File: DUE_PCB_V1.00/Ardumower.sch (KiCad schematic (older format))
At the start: 50 parts, among them J1 9V IN, J10 Sonar_R, J11 Sonar_C, J12 Sonar_L, J13 P_Right, J14 DS3231 RTC, J15 Button, J16 Button, J17 Button, J18 Button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

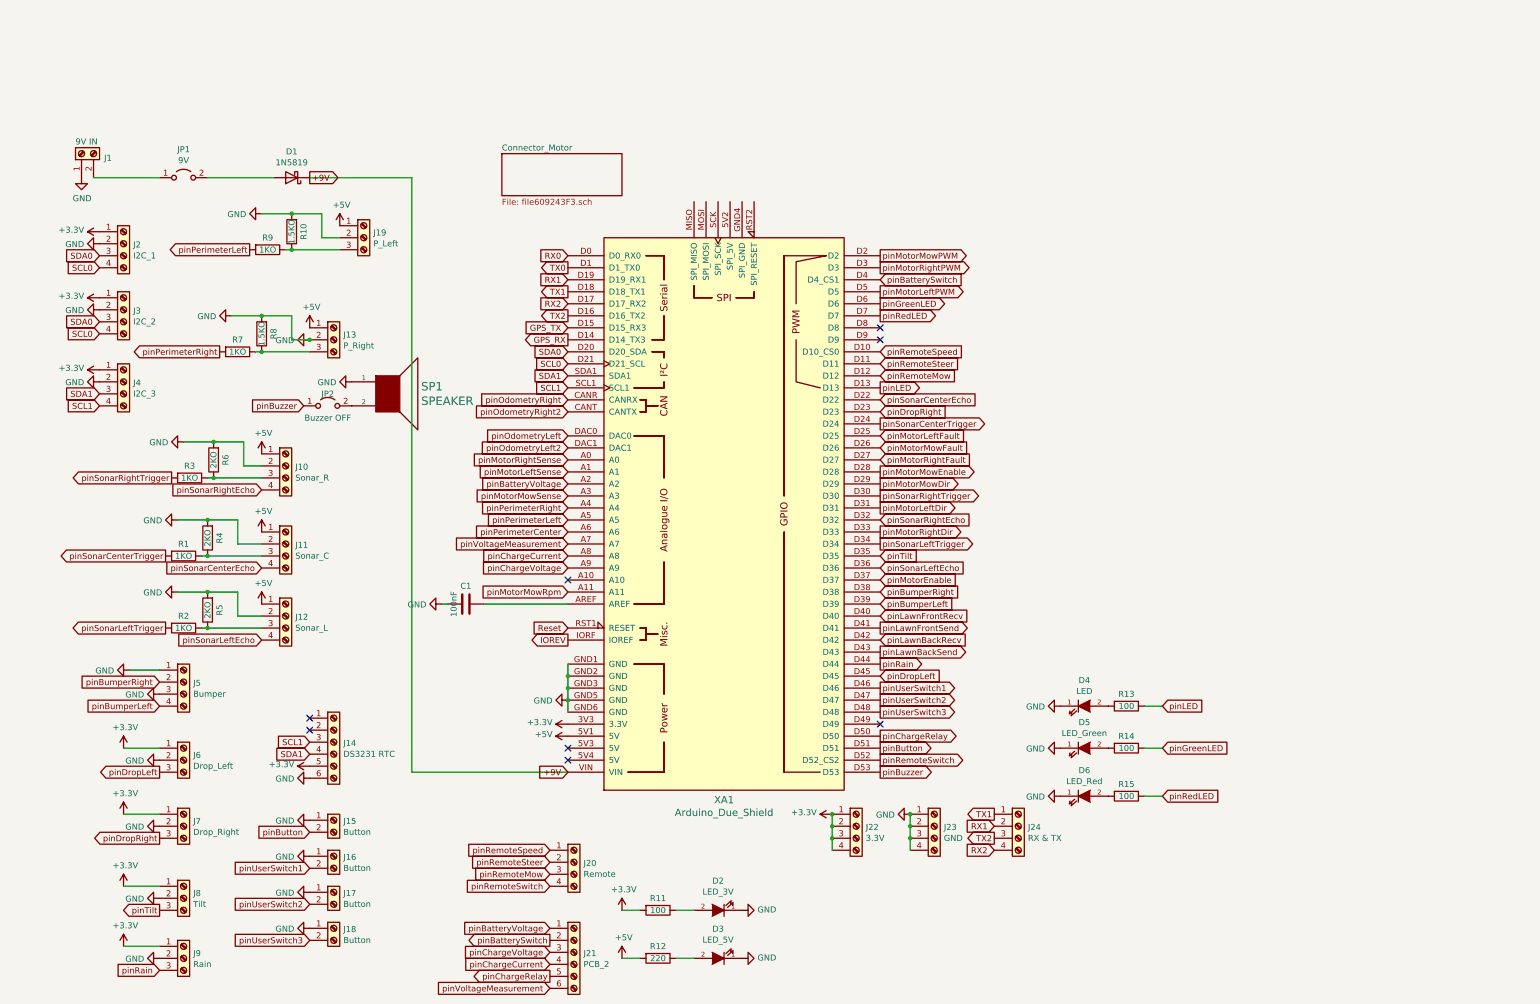
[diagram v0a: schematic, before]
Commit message: Add Power Source
Add Power Source for 5V & 3.3V
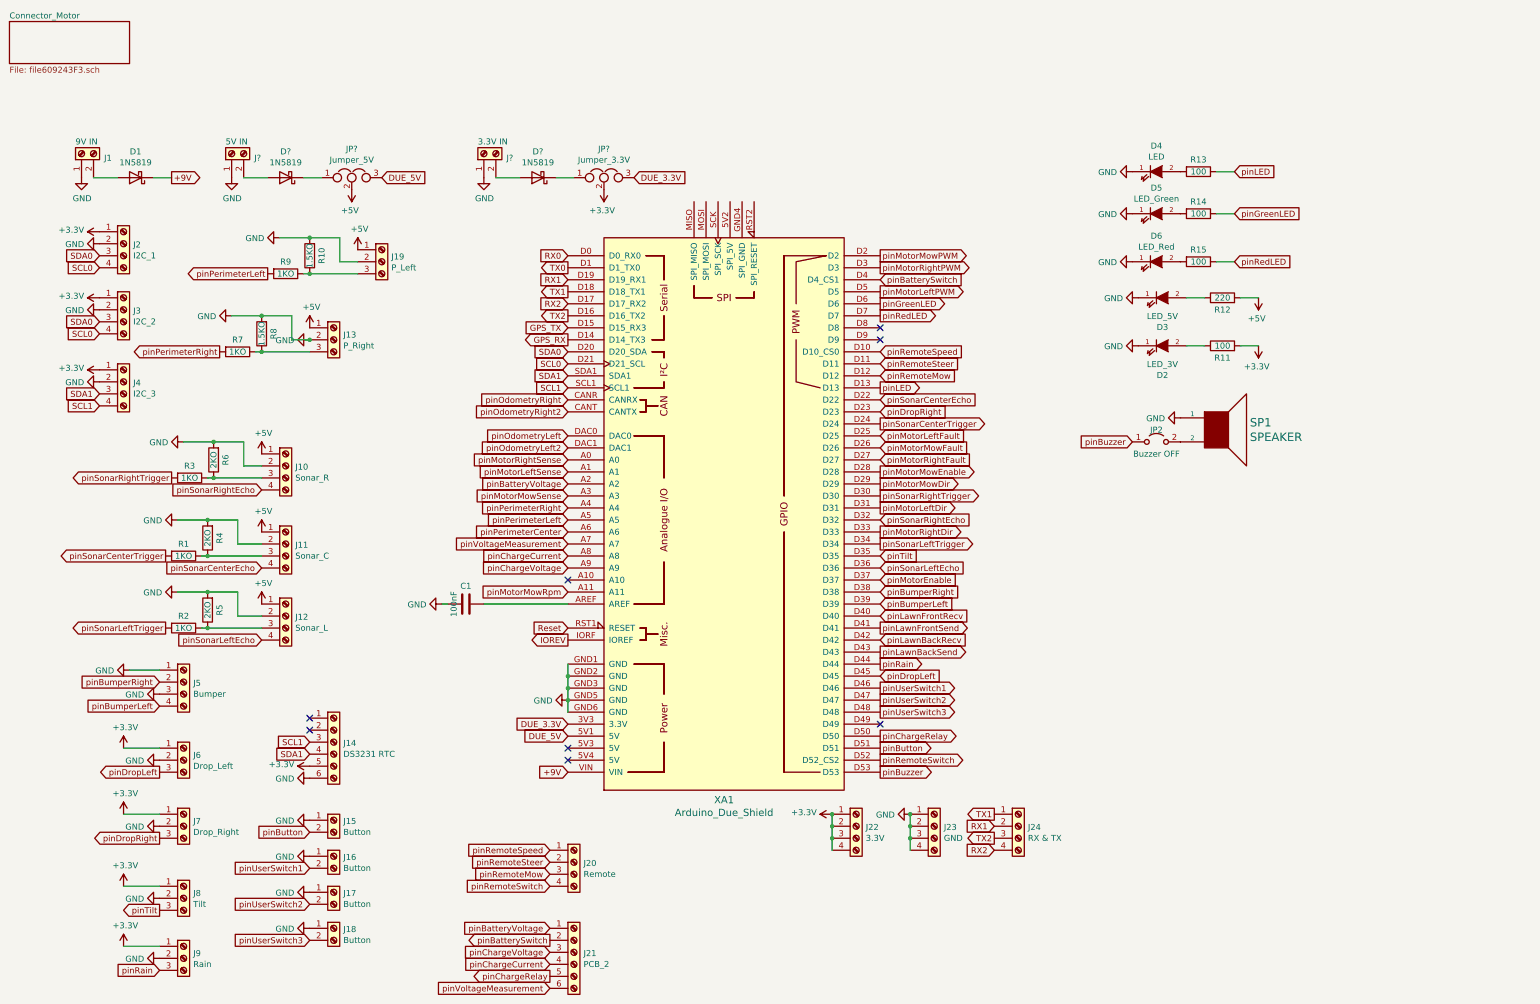
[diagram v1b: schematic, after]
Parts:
- removed JP1: 9V, Connector_PinHeader_2.54mm:PinHeader_1x02_P2.54mm_Vertical, symbol Jumper:Jumper_2_Open
- added D? (x2): 1N5819, Diode_THT:D_DO-41_SOD81_P10.16mm_Horizontal, symbol Diode:1N5819
- added J?: 5V IN, TerminalBlock:TerminalBlock_bornier-2_P5.08mm, symbol Connector:Screw_Terminal_01x02
- added J?: 3.3V IN, TerminalBlock:TerminalBlock_bornier-2_P5.08mm, symbol Connector:Screw_Terminal_01x02
- added JP?: Jumper_5V, symbol Device:Jumper_NC_Dual
- added JP?: Jumper_3.3V, symbol Device:Jumper_NC_Dual
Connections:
- net +3V3: now also JP?.2; no longer XA1.3V3 (3.3V)
- net +5V: now also JP?.2; no longer XA1.5V1 (5V)
- net GND: now also J?.1 (Pin_1), J?.1 (Pin_1)
- net at J1.2 (Pin_2): now also D1.2 (A)
- new net: D?.2 (A), J?.2 (Pin_2) (x2)
- new net: D?.1 (K), JP?.1 (x2)
- new net DUE_3.3V: JP?.3, XA1.3V3 (3.3V)
- new net DUE_5V: JP?.3, XA1.5V1 (5V)
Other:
- moved on the sheet: D1, D2, D3, D4, D5, D6, J19, JP2, R10, R11, R12, R13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

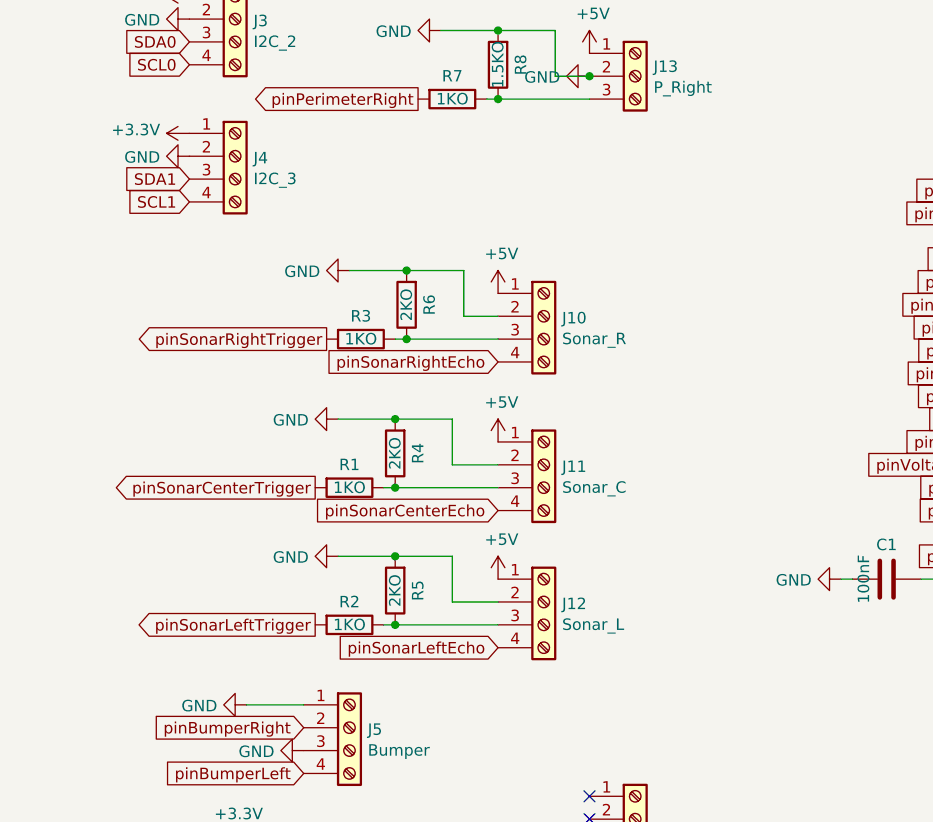
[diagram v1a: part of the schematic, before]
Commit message: Remove Sonar Resistors
Remove Sonar Resistors and change Power Source to 3.3V
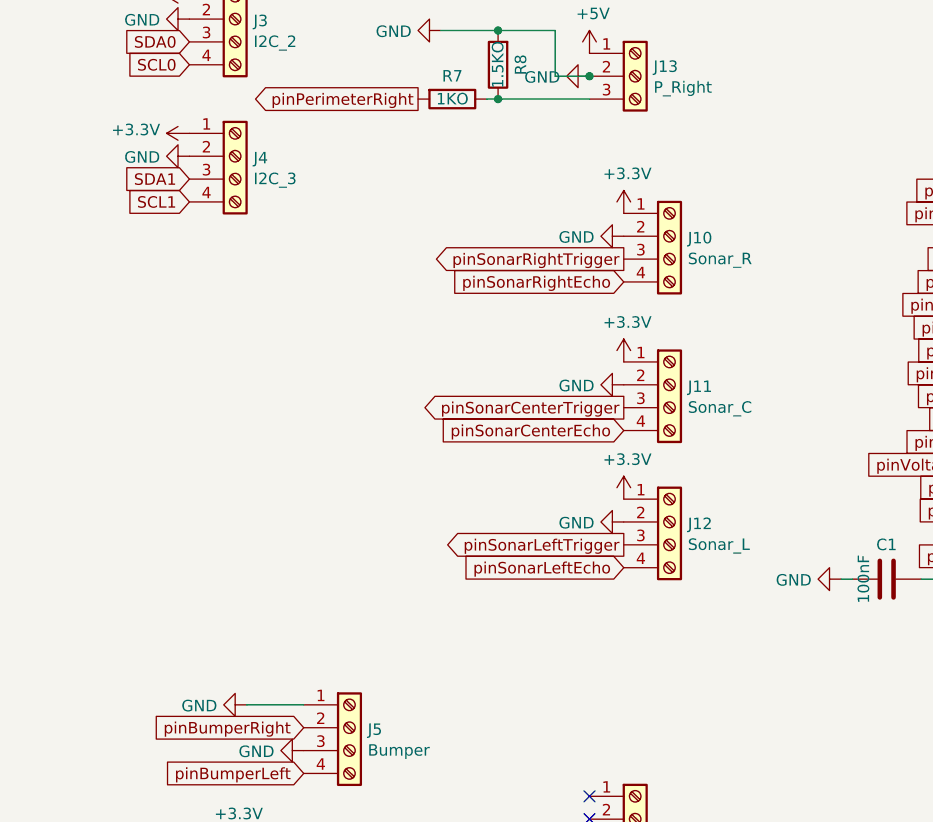
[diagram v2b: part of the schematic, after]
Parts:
- removed R1, R2, R3: 1KO, Resistor_THT:R_Axial_DIN0207_L6.3mm_D2.5mm_P2.54mm_Vertical, symbol Device:R
- removed R4, R5, R6: 2KO, Resistor_THT:R_Axial_DIN0207_L6.3mm_D2.5mm_P2.54mm_Vertical, symbol Device:R
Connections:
- net +3V3: now also J10.1 (Pin_1), J11.1 (Pin_1), J12.1 (Pin_1)
- net +5V: no longer J10.1 (Pin_1), J11.1 (Pin_1), J12.1 (Pin_1)
- net pinSonarCenterTrigger: now also J11.3 (Pin_3)
- net pinSonarLeftTrigger: now also J12.3 (Pin_3)
- net pinSonarRightTrigger: now also J10.3 (Pin_3)
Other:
- moved on the sheet: J10, J11, J12
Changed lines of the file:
@@
 L Connector:Screw_Terminal_01x04 J10
 U 1 1 60757000
-P 2500 3250
-F 0 "J10" H 2580 3242 50  0000 L CNN
-F 1 "Sonar_R" H 2580 3151 50  0000 L CNN
-F 2 "Connector_PinHeader_2.54mm:PinHeader_1x04_P2.54mm_Vertical" H 2500 3250 50  0001 C CNN
-F 3 "~" H 2500 3250 50  0001 C CNN
-	1    2500 3250
+P 3050 2900
+F 0 "J10" H 3130 2892 50  0000 L CNN
+F 1 "Sonar_R" H 3130 2801 50  0000 L CNN
+F 2 "Connector_PinHeader_2.54mm:PinHeader_1x04_P2.54mm_Vertical" H 3050 2900 50  0001 C CNN
+F 3 "~" H 3050 2900 50  0001 C CNN
+	1    3050 2900
 	1    0    0    -1
 $EndComp
@@
 L Connector:Screw_Terminal_01x04 J11
 U 1 1 607583E5
-P 2500 3900
-F 0 "J11" H 2580 3892 50  0000 L CNN
-F 1 "Sonar_C" H 2580 3801 50  0000 L CNN
-F 2 "Connector_PinHeader_2.54mm:PinHeader_1x04_P2.54mm_Vertical" H 2500 3900 50  0001 C CNN
-F 3 "~" H 2500 3900 50  0001 C CNN
-	1    2500 3900
+P 3050 3550
+F 0 "J11" H 3130 3542 50  0000 L CNN
+F 1 "Sonar_C" H 3130 3451 50  0000 L CNN
+F 2 "Connector_PinHeader_2.54mm:PinHeader_1x04_P2.54mm_Vertical" H 3050 3550 50  0001 C CNN
+F 3 "~" H 3050 3550 50  0001 C CNN
+	1    3050 3550
 	1    0    0    -1
 $EndComp
@@
 L Connector:Screw_Terminal_01x04 J12
 U 1 1 60758E5B
-P 2500 4500
-F 0 "J12" H 2580 4492 50  0000 L CNN
-F 1 "Sonar_L" H 2580 4401 50  0000 L CNN
-F 2 "Connector_PinHeader_2.54mm:PinHeader_1x04_P2.54mm_Vertical" H 2500 4500 50  0001 C CNN
-F 3 "~" H 2500 4500 50  0001 C CNN
-	1    2500 4500
-	1    0    0    -1
-$EndComp
-$Comp
-L power:+5V #PWR024
-U 1 1 6075A993
-P 2300 3800
-F 0 "#PWR024" H 2300 3650 50  0001 C CNN
-F 1 "+5V" H 2315 3973 50  0000 C CNN
-F 2 "" H 2300 3800 50  0001 C CNN
-F 3 "" H 2300 3800 50  0001 C CNN
-	1    2300 3800
-	1    0    0    -1
-$EndComp
-$Comp
-L power:+5V #PWR025
-U 1 1 6075B07F
-P 2300 4400
-F 0 "#PWR025" H 2300 4250 50  0001 C CNN
-F 1 "+5V" H 2315 4573 50  0000 C CNN
-F 2 "" H 2300 4400 50  0001 C CNN
-F 3 "" H 2300 4400 50  0001 C CNN
-	1    2300 4400
-	1    0    0    -1
-$EndComp
-Text GLabel 2300 4100 0    50   Input ~ 0
+P 3050 4150
+F 0 "J12" H 3130 4142 50  0000 L CNN
+F 1 "Sonar_L" H 3130 4051 50  0000 L CNN
+F 2 "Connector_PinHeader_2.54mm:PinHeader_1x04_P2.54mm_Vertical" H 3050 4150 50  0001 C CNN
+F 3 "~" H 3050 4150 50  0001 C CNN
+	1    3050 4150
+	1    0    0    -1
+$EndComp
+Text GLabel 2850 3750 0    50   Input ~ 0
 pinSonarCenterEcho
-Text GLabel 2300 3450 0    50   Input ~ 0
+Text GLabel 2850 3100 0    50   Input ~ 0
 pinSonarRightEcho
-Text GLabel 2300 4700 0    50   Input ~ 0
+Text GLabel 2850 4350 0    50   Input ~ 0
 pinSonarLeftEcho
 $Comp
@@
 L power:GND #PWR018
 U 1 1 6097F3DC
-P 1600 3700
-F 0 "#PWR018" H 1600 3450 50  0001 C CNN
-F 1 "GND" V 1605 3572 50  0000 R CNN
-F 2 "" H 1600 3700 50  0001 C CNN
-F 3 "" H 1600 3700 50  0001 C CNN
-	1    1600 3700
+P 2850 3550
+F 0 "#PWR018" H 2850 3300 50  0001 C CNN
+F 1 "GND" V 2855 3422 50  0000 R CNN
+F 2 "" H 2850 3550 50  0001 C CNN
+F 3 "" H 2850 3550 50  0001 C CNN
+	1    2850 3550
 	0    1    1    0
 $EndComp
@@
 NoConn ~ 7450 5400
 NoConn ~ 7450 2200
-Wire Wire Line
-	2100 3700 2100 3900
-Wire Wire Line
-	2100 3900 2300 3900
 $Comp
 L power:GND #PWR019
 U 1 1 60A92EB8
-P 1600 4300
-F 0 "#PWR019" H 1600 4050 50  0001 C CNN
-F 1 "GND" V 1605 4172 50  0000 R CNN
-F 2 "" H 1600 4300 50  0001 C CNN
-F 3 "" H 1600 4300 50  0001 C CNN
-	1    1600 4300
-	0    1    1    0
-$EndComp
-Wire Wire Line
-	2100 4300 2100 4500
-Wire Wire Line
-	2100 4500 2300 4500
+P 2850 4150
+F 0 "#PWR019" H 2850 3900 50  0001 C CNN
+F 1 "GND" V 2855 4022 50  0000 R CNN
+F 2 "" H 2850 4150 50  0001 C CNN
+F 3 "" H 2850 4150 50  0001 C CNN
+	1    2850 4150
+	0    1    1    0
+$EndComp
 $Comp
 L power:GND #PWR020
 U 1 1 60A9B8D5
-P 1650 3050
-F 0 "#PWR020" H 1650 2800 50  0001 C CNN
-F 1 "GND" V 1655 2922 50  0000 R CNN
-F 2 "" H 1650 3050 50  0001 C CNN
-F 3 "" H 1650 3050 50  0001 C CNN
-	1    1650 3050
-	0    1    1    0
-$EndComp
-Wire Wire Line
-	2150 3050 2150 3250
-Wire Wire Line
-	2150 3250 2300 3250
-$Comp
-L power:+5V #PWR023
-U 1 1 60AAE1DB
-P 2300 3150
-F 0 "#PWR023" H 2300 3000 50  0001 C CNN
-F 1 "+5V" H 2315 3323 50  0000 C CNN
-F 2 "" H 2300 3150 50  0001 C CNN
-F 3 "" H 2300 3150 50  0001 C CNN
-	1    2300 3150
-	1    0    0    -1
+P 2850 2900
+F 0 "#PWR020" H 2850 2650 50  0001 C CNN
+F 1 "GND" V 2855 2772 50  0000 R CNN
+F 2 "" H 2850 2900 50  0001 C CNN
+F 3 "" H 2850 2900 50  0001 C CNN
+	1    2850 2900
+	0    1    1    0
 $EndComp
 Text GLabel 7450 1500 2    50   Output ~ 0
@@
 Text GLabel 4850 4300 0    50   Input ~ 0
 pinMotorMowRpm
-Wire Wire Line
-	2150 3050 1900 3050
-Wire Wire Line
-	1650 3050 1900 3050
-Connection ~ 1900 3050
-Wire Wire Line
-	2300 3350 1900 3350
-Connection ~ 1900 3350
-$Comp
-L Device:R R6
-U 1 1 60A9C277
-P 1900 3200
-F 0 "R6" V 1800 3200 50  0000 C CNN
-F 1 "2KO" V 1900 3200 50  0000 C CNN
-F 2 "Resistor_THT:R_Axial_DIN0207_L6.3mm_D2.5mm_P2.54mm_Vertical" V 1830 3200 50  0001 C CNN
-F 3 "~" H 1900 3200 50  0001 C CNN
-	1    1900 3200
-	-1   0    0    1
-$EndComp
-Wire Wire Line
-	1850 3350 1900 3350
-$Comp
-L Device:R R3
-U 1 1 60A9C26D
-P 1700 3350
-F 0 "R3" V 1600 3350 50  0000 C CNN
-F 1 "1KO" V 1700 3350 50  0000 C CNN
-F 2 "Resistor_THT:R_Axial_DIN0207_L6.3mm_D2.5mm_P2.54mm_Vertical" V 1630 3350 50  0001 C CNN
-F 3 "~" H 1700 3350 50  0001 C CNN
-	1    1700 3350
-	0    1    1    0
-$EndComp
-Text GLabel 1550 3350 0    50   Output ~ 0
+Text GLabel 2850 3000 0    50   Output ~ 0
 pinSonarRightTrigger
-Wire Wire Line
-	1600 3700 1850 3700
-Wire Wire Line
-	2100 3700 1850 3700
-Connection ~ 1850 3700
-Wire Wire Line
-	2300 4000 1850 4000
-$Comp
-L Device:R R4
-U 1 1 60A59EEA
-P 1850 3850
-F 0 "R4" V 1750 3850 50  0000 C CNN
-F 1 "2KO" V 1850 3850 50  0000 C CNN
-F 2 "Resistor_THT:R_Axial_DIN0207_L6.3mm_D2.5mm_P2.54mm_Vertical" V 1780 3850 50  0001 C CNN
-F 3 "~" H 1850 3850 50  0001 C CNN
-	1    1850 3850
-	-1   0    0    1
-$EndComp
-$Comp
-L Device:R R1
-U 1 1 60A4F6FF
-P 1650 4000
-F 0 "R1" V 1550 4000 50  0000 C CNN
-F 1 "1KO" V 1650 4000 50  0000 C CNN
-F 2 "Resistor_THT:R_Axial_DIN0207_L6.3mm_D2.5mm_P2.54mm_Vertical" V 1580 4000 50  0001 C CNN
-F 3 "~" H 1650 4000 50  0001 C CNN
-	1    1650 4000
-	0    1    1    0
-$EndComp
-Text GLabel 1500 4000 0    50   Output ~ 0
+Text GLabel 2850 3650 0    50   Output ~ 0
 pinSonarCenterTrigger
-Wire Wire Line
-	1600 4300 1850 4300
-Wire Wire Line
-	2100 4300 1850 4300
-Connection ~ 1850 4300
-Wire Wire Line
-	2300 4600 1850 4600
-$Comp
-L Device:R R5
-U 1 1 60A9384A
-P 1850 4450
-F 0 "R5" V 1750 4450 50  0000 C CNN
-F 1 "2KO" V 1850 4450 50  0000 C CNN
-F 2 "Resistor_THT:R_Axial_DIN0207_L6.3mm_D2.5mm_P2.54mm_Vertical" V 1780 4450 50  0001 C CNN
-F 3 "~" H 1850 4450 50  0001 C CNN
-	1    1850 4450
-	-1   0    0    1
-$EndComp
-$Comp
-L Device:R R2
-U 1 1 60A93840
-P 1650 4600
-F 0 "R2" V 1550 4600 50  0000 C CNN
-F 1 "1KO" V 1650 4600 50  0000 C CNN
-F 2 "Resistor_THT:R_Axial_DIN0207_L6.3mm_D2.5mm_P2.54mm_Vertical" V 1580 4600 50  0001 C CNN
-F 3 "~" H 1650 4600 50  0001 C CNN
-	1    1650 4600
-	0    1    1    0
-$EndComp
-Text GLabel 1500 4600 0    50   Output ~ 0
+Text GLabel 2850 4250 0    50   Output ~ 0
 pinSonarLeftTrigger
-Wire Wire Line
-	1800 4000 1850 4000
-Connection ~ 1850 4000
-Wire Wire Line
-	1800 4600 1850 4600
-Connection ~ 1850 4600
 $Comp
 L power:GND #PWR021
@@
 	1    0    0    -1
 $EndComp
+$Comp
+L power:+3.3V #PWR?
+U 1 1 60CD5141
+P 2850 2800
+F 0 "#PWR?" H 2850 2650 50  0001 C CNN
+F 1 "+3.3V" H 2865 2973 50  0000 C CNN
+F 2 "" H 2850 2800 50  0001 C CNN
+F 3 "" H 2850 2800 50  0001 C CNN
+	1    2850 2800
+	1    0    0    -1
+$EndComp
+$Comp
+L power:+3.3V #PWR?
+U 1 1 60CD78FD
+P 2850 3450
+F 0 "#PWR?" H 2850 3300 50  0001 C CNN
+F 1 "+3.3V" H 2865 3623 50  0000 C CNN
+F 2 "" H 2850 3450 50  0001 C CNN
+F 3 "" H 2850 3450 50  0001 C CNN
+	1    2850 3450
+	1    0    0    -1
+$EndComp
+$Comp
+L power:+3.3V #PWR?
+U 1 1 60CDB03B
+P 2850 4050
+F 0 "#PWR?" H 2850 3900 50  0001 C CNN
+F 1 "+3.3V" H 2865 4223 50  0000 C CNN
+F 2 "" H 2850 4050 50  0001 C CNN
+F 3 "" H 2850 4050 50  0001 C CNN
+	1    2850 4050
+	1    0    0    -1
+$EndComp
